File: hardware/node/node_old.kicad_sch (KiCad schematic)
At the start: 51 parts, among them IC1 MCP73844-840I_MS, IC2 NEO-M9N-00B, J1 USB_C_Receptacle, J2 OMEGA2_HEADER, Q1 IRF7404, Q2 AO3400A, Q3 S8550, SW1 SW_POWER, U3 ADS1115IDGS, U4 Omega2S

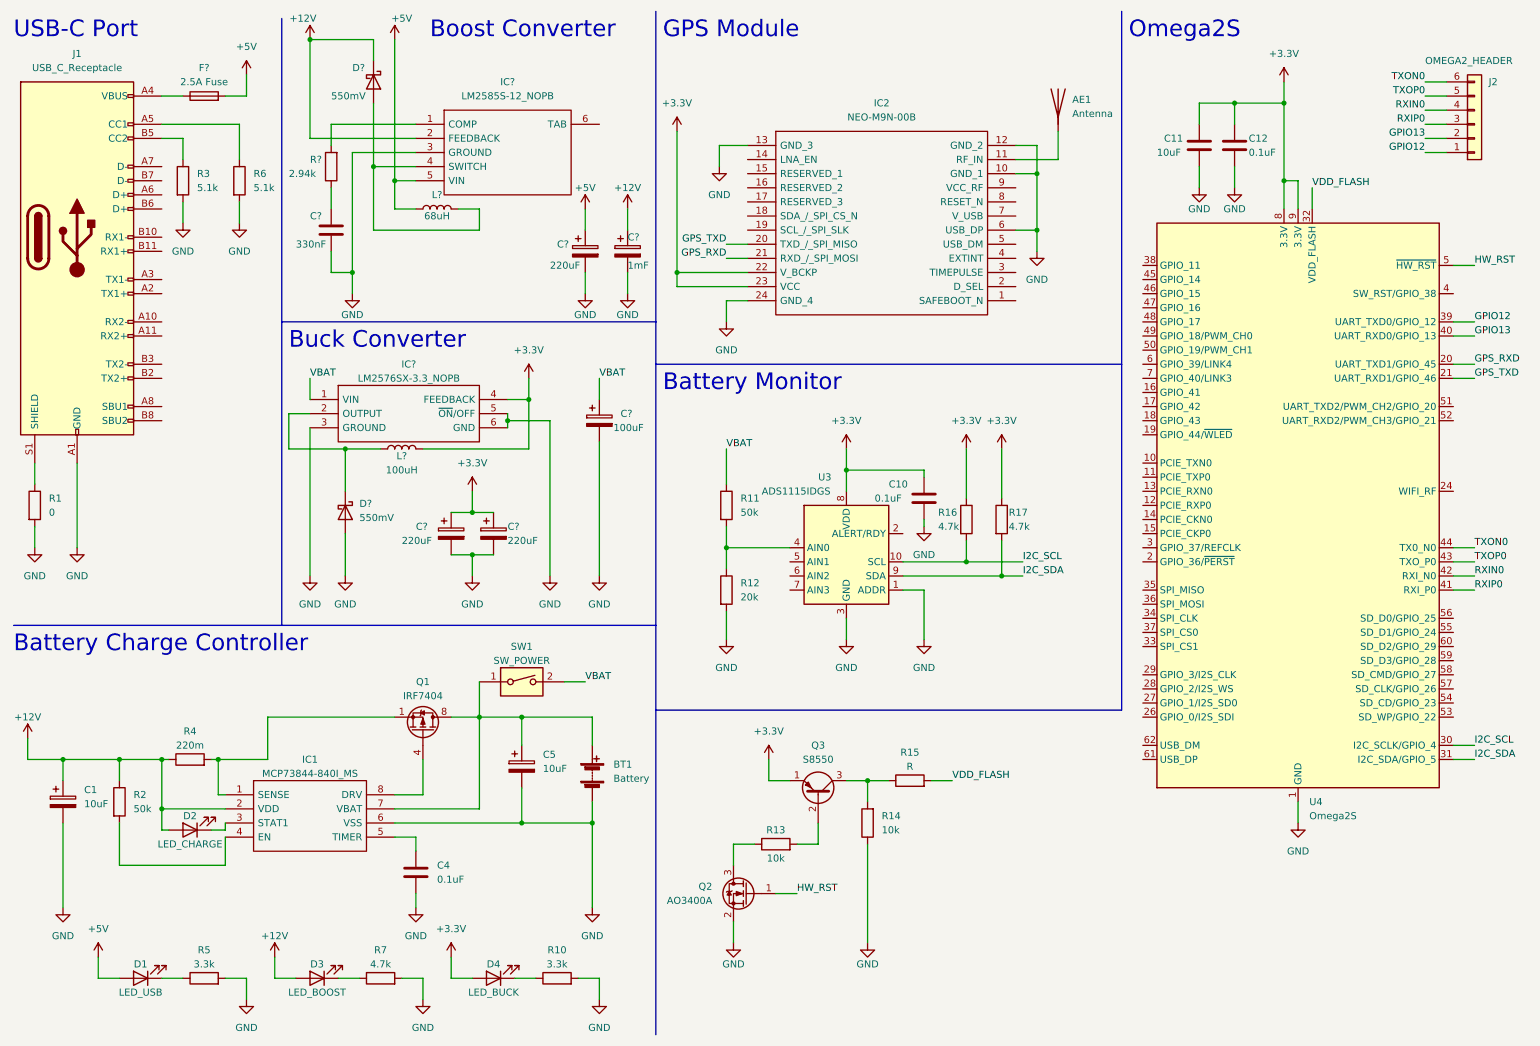
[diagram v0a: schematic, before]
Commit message: fix schematic naming, remove hard reset circuit
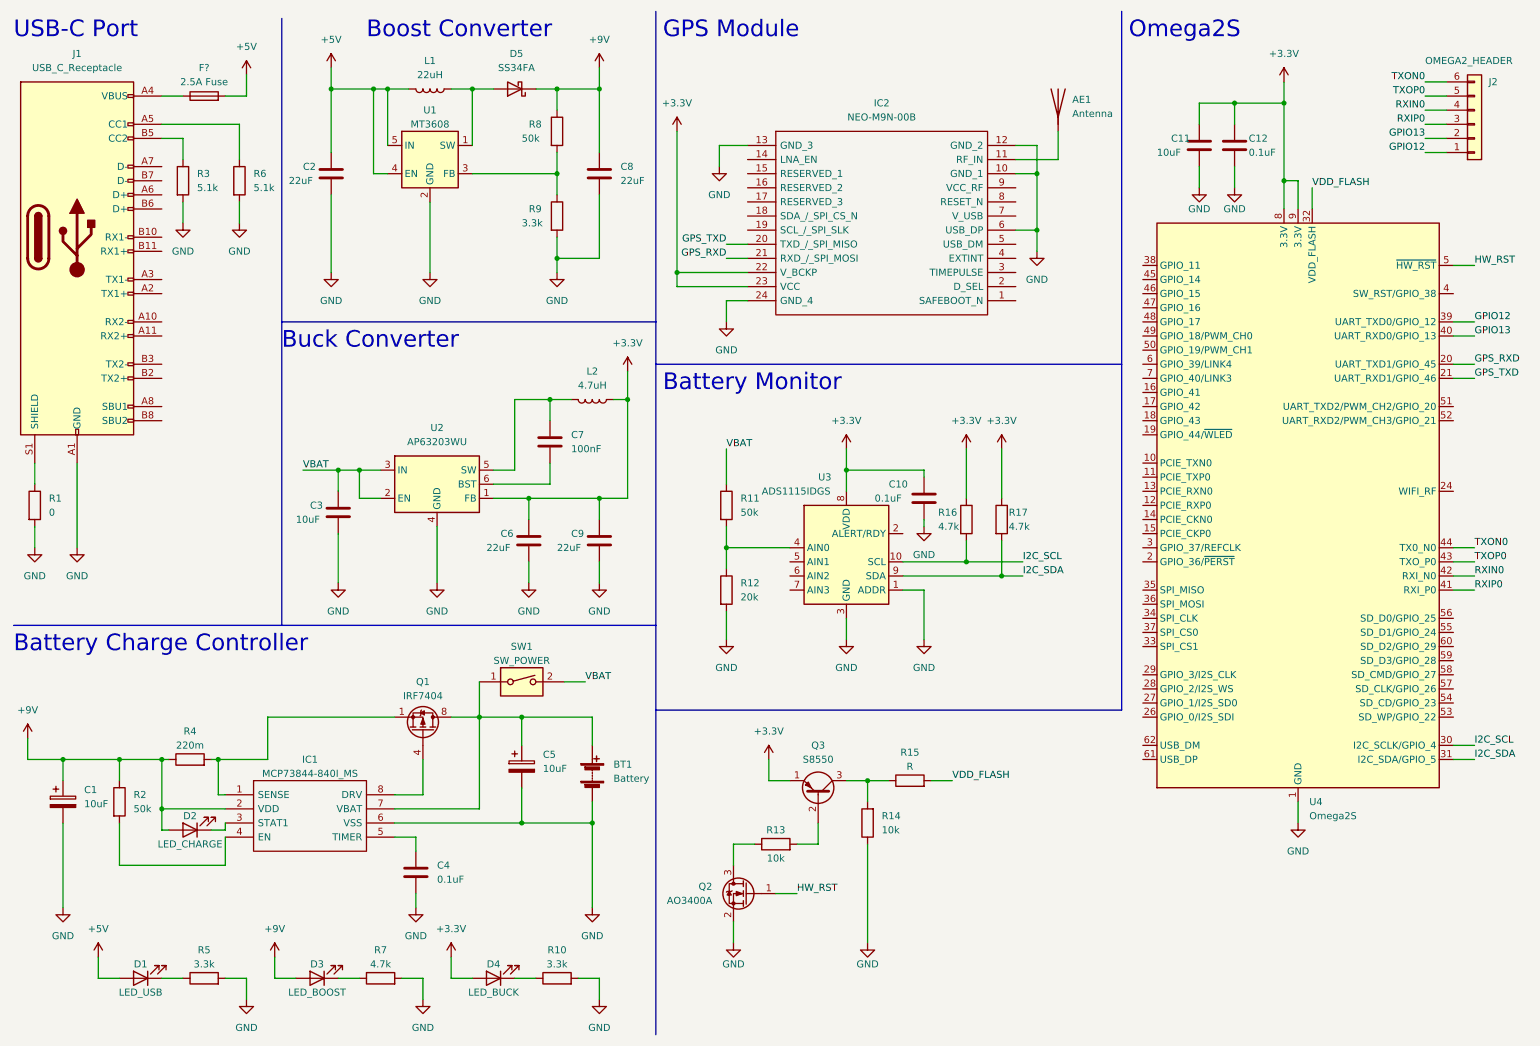
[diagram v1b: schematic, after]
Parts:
- removed C?: 1mF, symbol Device:C_Polarized
- removed C? (x3): 220uF, symbol Device:C_Polarized
- removed C?: 100uF, symbol Device:C_Polarized
- removed C?: 330nF, symbol Device:C
- removed D? (x2): 550mV, symbol Device:D_Schottky
- removed IC?: LM2585S-12_NOPB, TO170P1435X465-6N, symbol Boost_Converter_12v:LM2585S-12_NOPB
- removed IC?: LM2576SX-3.3_NOPB, KTT0005B, symbol Buck_Converter:LM2576SX-3.3_NOPB
- removed L?: 68uH, symbol Device:L
- removed L?: 100uH, symbol Device:L
- removed R?: 2.94k, symbol Device:R
- added C2, C6, C8, C9: 22uF, symbol Device:C
- added C3: 10uF, symbol Device:C
- added C7: 100nF, symbol Device:C
- added D5: SS34FA, symbol Device:D_Schottky
- added L1: 22uH, symbol Device:L
- added L2: 4.7uH, symbol Device:L
- added R8: 50k, symbol Device:R
- added R9: 3.3k, symbol Device:R
- added U1: MT3608, Package_TO_SOT_SMD:SOT-23-6, symbol Regulator_Switching:MT3608
- added U2: AP63203WU, Package_TO_SOT_SMD:TSOT-23-6, symbol Regulator_Switching:AP63203WU
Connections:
- net +3.3V: now also C6.1, C9.1, L2.1, U2.1 (FB)
- net +5V: now also C2.1, L1.2, U1.4 (EN), U1.5 (IN)
- net GND: now also C2.2, C3.2, C6.2, C8.2, C9.2, R9.2, U1.2 (GND), U2.4 (GND)
- net VBAT: now also C3.1, U2.2 (EN), U2.3 (IN)
- net +12V renamed +9V
- net +9V: now also C8.1, D5.1 (K), R8.1
- new net: D5.2 (A), L1.1, U1.1 (SW)
- new net: R8.2, R9.1, U1.3 (FB)
- new net: C7.1, L2.2, U2.5 (SW)
- new net: C7.2, U2.6 (BST)
